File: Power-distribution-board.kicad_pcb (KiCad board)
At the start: 2 copper layers, 79 parts, among them J1 178.6165.0001 breaker, J10 2606-1104/020-000, J12 2606-1104/020-000, J13 2606-1104/020-000, J15 2606-1104/020-000, J16 2606-1104/020-000, J2 178.6165.0001 breaker, J3 178.6165.0001 breaker, J4 178.6165.0001 breaker, J5 178.6165.0001 breaker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

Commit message: work on pcb editor
changed layout of components, changed to 4 layer pcb, set minimum trace width 0.2mm
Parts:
- moved J10 212.6 mm to (254.2, 91.3), turned to 90 degrees
- moved J13 182.2 mm to (251.8, 54.4), turned to 90 degrees
- moved J6 180.9 mm to (246.2, 66.3), turned to 90 degrees
- moved J5 169.5 mm to (237.4, 66.3), turned to 90 degrees
- moved J4 169.4 mm to (246.6, 90.1), turned to 90 degrees
- moved J2 157.7 mm to (230.5, 56.1), turned to 180 degrees
- moved J12 142.6 mm to (221.9, 111.5)
- moved J3 139.9 mm to (208.3, 55.9), turned to 180 degrees
- moved J16 135.7 mm to (238.2, 50.1)
- moved J15 135.6 mm to (253.0, 126.6), turned to 90 degrees
- moved U3 124.1 mm to (214.7, 74.2), turned to 180 degrees
- moved U14 106.6 mm to (205.1, 69.0), turned to 180 degrees
- moved U12 104.5 mm to (204.1, 87.1), turned to 180 degrees
- moved U13 102.7 mm to (203.9, 81.6), turned to 180 degrees
- moved U15 101.2 mm to (215.0, 87.7), turned to 180 degrees
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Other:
- copper layers 2 -> 4

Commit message: set layout
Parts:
- moved U15 134.3 mm to (81.6, 103.1)
- moved U16 120.5 mm to (100.0, 118.9)
- moved U3 120.4 mm to (94.4, 78.3)
- moved J5 118.0 mm to (132.2, 119.6), turned to 180 degrees
- moved R45 117.9 mm to (64.2, 133.5)
- moved J9 117.4 mm to (63.0, 140.9), turned to 0 degrees
- moved U4 116.6 mm to (98.0, 141.7)
- moved U2 113.1 mm to (80.5, 138.7), turned to 180 degrees
- moved U17 108.2 mm to (94.8, 99.0)
- moved R46 104.3 mm to (61.4, 133.5)
- moved U1 100.4 mm to (70.4, 75.1), turned to 0 degrees
- moved R24 97.9 mm to (143.3, 98.9), turned to 0 degrees
- moved C5 97.7 mm to (53.6, 134.2), turned to 0 degrees
- moved U12 96.7 mm to (108.2, 99.1), turned to -90 degrees
- moved R5 94.5 mm to (56.7, 124.1), turned to 180 degrees
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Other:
- board outline added: 139.2 x 107.7 mm

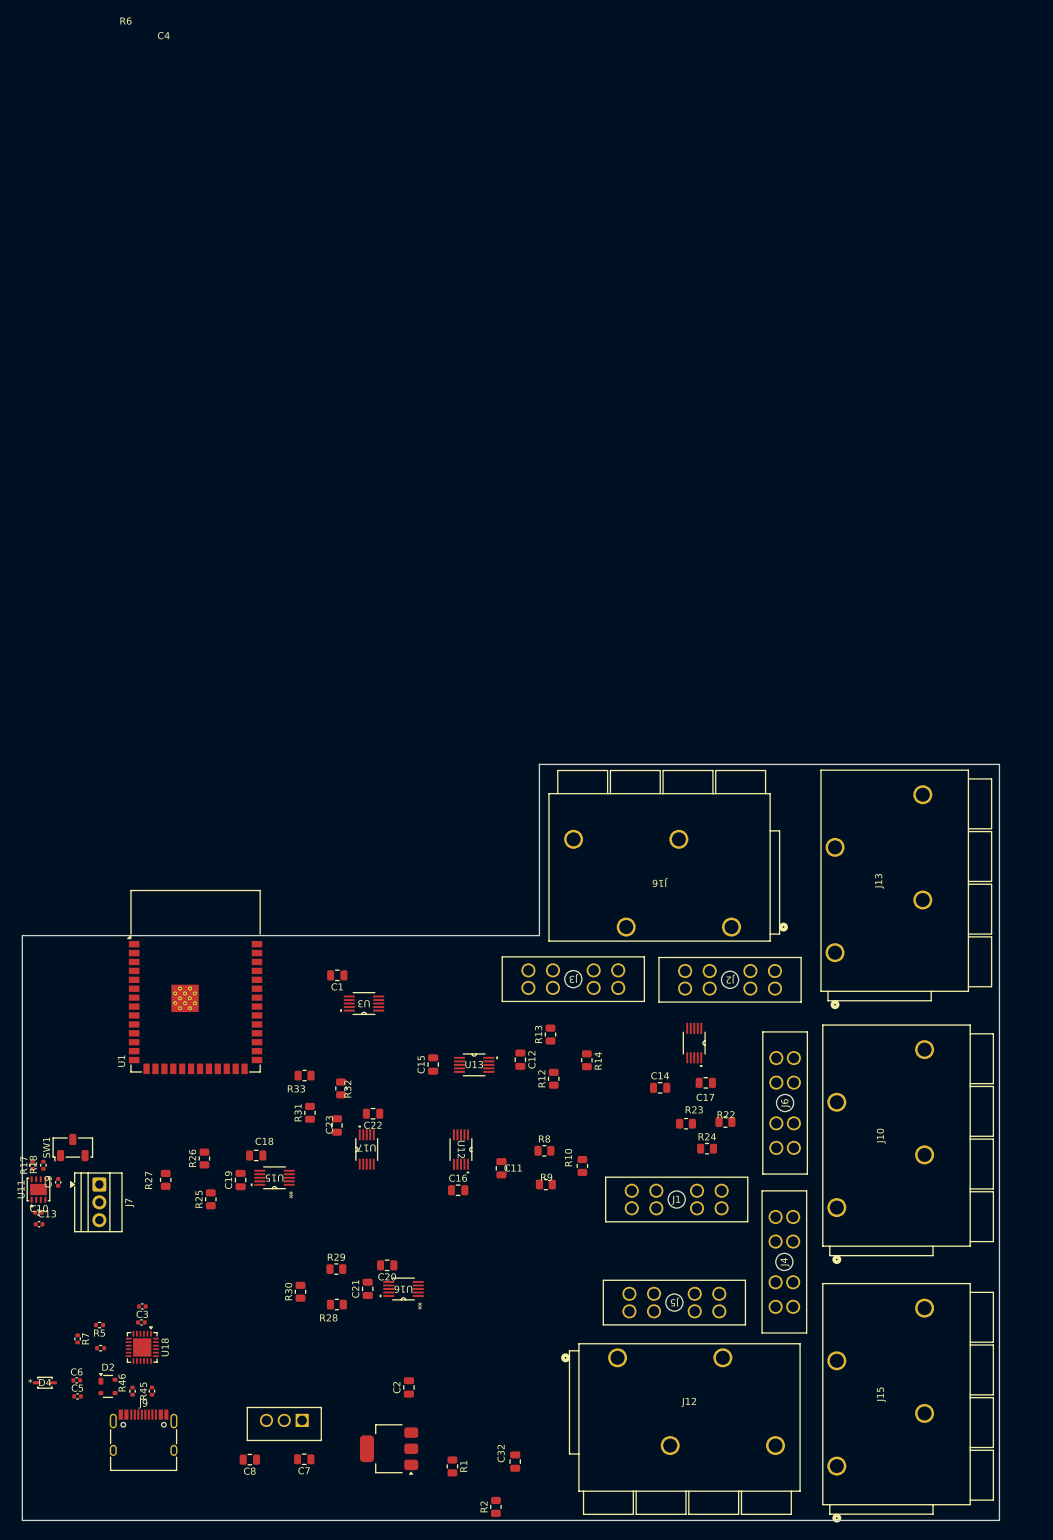
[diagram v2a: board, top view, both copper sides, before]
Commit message: update layout
added board edge and planes
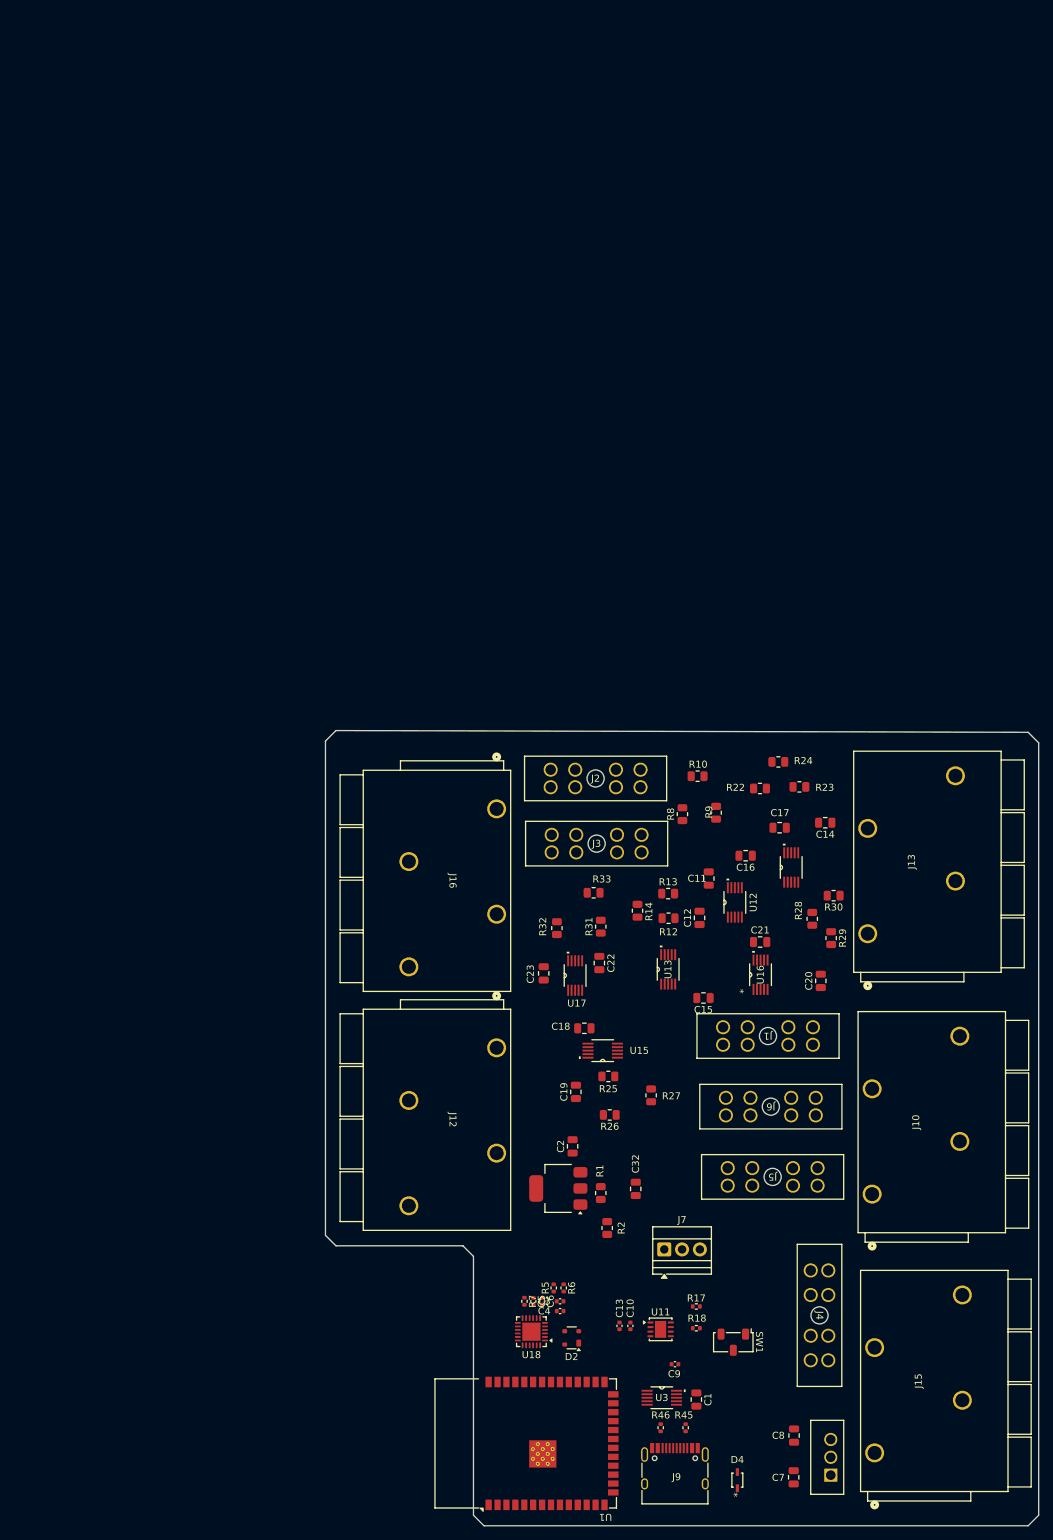
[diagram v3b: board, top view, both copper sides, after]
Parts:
- moved D4 99.6 mm to (147.6, 146.2), turned to 90 degrees
- moved SW1 98.1 mm to (147.0, 126.5), turned to -90 degrees
- moved R17 96.7 mm to (141.7, 121.4), turned to 0 degrees
- moved R18 95.9 mm to (141.7, 124.5), turned to 0 degrees
- moved R30 94.6 mm to (161.3, 62.9), turned to 180 degrees
- moved C9 91.6 mm to (138.7, 129.6), turned to 180 degrees
- moved U11 90.8 mm to (136.6, 124.7), turned to 0 degrees
- moved R28 87.2 mm to (158.2, 66.2), turned to 90 degrees
- moved C10 85.9 mm to (132.3, 124.2), turned to -90 degrees
- moved R29 84.8 mm to (160.9, 68.9), turned to -90 degrees
- moved C13 83.9 mm to (130.8, 124.2), turned to -90 degrees
- moved J7 81.0 mm to (137.2, 113.3), turned to 0 degrees
- moved U1 80.9 mm to (117.4, 140.9), turned to 90 degrees
- moved U2 79.4 mm to (159.9, 140.4), turned to 90 degrees
- moved C1 79.2 mm to (141.7, 134.7), turned to -90 degrees
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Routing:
- added copper zone on In1.Cu, net GND
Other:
- board size 139.2 x 107.7 mm -> 101.6 x 113.3 mm

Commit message: rearrangement
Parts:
- moved R5 7.55 mm to (120.8, 111.2)
- moved R6 7.55 mm to (122.2, 111.2)
- moved R7 6.57 mm to (114.3, 114.8)
- moved C5 6.04 mm to (117.1, 114.8)
- moved C6 6.00 mm to (119.9, 114.7)
- moved U18 5.62 mm to (115.9, 119.9)
- moved U1 2.74 mm to (116.5, 138.3)
- moved C3 2.60 mm to (121.9, 118.1)
- moved C4 2.60 mm to (121.9, 119.5)
- moved J16 2.02 mm to (113.3, 48.5)
- moved D2 1.28 mm to (123.4, 124.7)
- moved C15 1.02 mm to (142.7, 76.5)
- moved J9 0.16 mm to (138.8, 145.6)
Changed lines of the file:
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@@
 	)
 	(footprint "Connector_USB:USB_C_Receptacle_HRO_TYPE-C-31-M-12"
-		(locked yes)
 		(layer "F.Cu")
-		(at 138.684 145.635)
+		(at 138.842 145.602)
 		(descr "USB Type-C receptacle for USB 2.0 and PD, http://www.krhro.com/uploads/soft/180320/1-1P320120243.pdf")
 		(tags "usb usb-c 2.0 pd")
@@
 	)
 	(footprint "Package_DFN_QFN:QFN-24-1EP_4x4mm_P0.5mm_EP2.6x2.6mm"
-		(locked yes)
 		(layer "F.Cu")
-		(at 118.2336 125.0084 180)
+		(at 115.9185 119.884 180)
 		(descr "QFN, 24 Pin (http://ww1.microchip.com/downloads/en/PackagingSpec/00000049BQ.pdf#page=278), generated with kicad-footprint-generator ipc_noLead_generator.py")
 		(tags "QFN NoLead")
 		(property "Reference" "U18"
-			(at 0 -3.3 0)
+			(at -0.1595 -3.814 0)
 			(layer "F.SilkS")
 			(effects
@@
 	)
 	(footprint "Resistor_SMD:R_0402_1005Metric"
-		(locked yes)
 		(layer "F.Cu")
-		(at 121.412 118.7704 90)
+		(at 120.7502 111.25 90)
 		(descr "Resistor SMD 0402 (1005 Metric), square (rectangular) end terminal, IPC-7351 nominal, (Body size source: IPC-SM-782 page 72, https://www.pcb-3d.com/wordpress/wp-content/uploads/ipc-sm-782a_amendment_1_and_2.pdf), generated with kicad-footprint-generator")
 		(tags "resistor")
@@
 	)
 	(footprint "Resistor_SMD:R_0402_1005Metric"
-		(locked yes)
 		(layer "F.Cu")
-		(at 117.2478 120.6754 -90)
+		(at 114.3 114.808 -90)
 		(descr "Resistor SMD 0402 (1005 Metric), square (rectangular) end terminal, IPC-7351 nominal, (Body size source: IPC-SM-782 page 72, https://www.pcb-3d.com/wordpress/wp-content/uploads/ipc-sm-782a_amendment_1_and_2.pdf), generated with kicad-footprint-generator")
 		(tags "resistor")
 		(property "Reference" "R7"
-			(at 0 -1.17 90)
+			(at -2.286 0 270)
 			(layer "F.SilkS")
 			(effects
@@
 	)
 	(footprint "Resistor_SMD:R_0402_1005Metric"
-		(locked yes)
 		(layer "F.Cu")
-		(at 122.8358 118.7704 -90)
+		(at 122.174 111.25 -90)
 		(descr "Resistor SMD 0402 (1005 Metric), square (rectangular) end terminal, IPC-7351 nominal, (Body size source: IPC-SM-782 page 72, https://www.pcb-3d.com/wordpress/wp-content/uploads/ipc-sm-782a_amendment_1_and_2.pdf), generated with kicad-footprint-generator")
 		(tags "resistor")
@@
 	)
 	(footprint "Package_TO_SOT_SMD:SOT-143"
-		(locked yes)
 		(layer "F.Cu")
-		(at 123.9788 125.8824 180)
+		(at 123.444 124.714 180)
 		(descr "SOT-143 https://www.nxp.com/docs/en/package-information/SOT143B.pdf")
 		(tags "SOT-143")
@@
 	)
 	(footprint "Capacitor_SMD:C_0402_1005Metric"
-		(locked yes)
 		(layer "F.Cu")
-		(at 122.3278 122.0724 180)
+		(at 121.92 119.507 180)
 		(descr "Capacitor SMD 0402 (1005 Metric), square (rectangular) end terminal, IPC-7351 nominal, (Body size source: IPC-SM-782 page 76, https://www.pcb-3d.com/wordpress/wp-content/uploads/ipc-sm-782a_amendment_1_and_2.pdf), generated with kicad-footprint-generator")
 		(tags "capacitor")
 		(property "Reference" "C4"
-			(at 2.258 0 0)
+			(at -2.286 0.127 0)
 			(layer "F.SilkS")
 			(effects
@@
 		(tags "INA220BIDGSR ")
 		(property "Reference" "U14"
-			(at -0.5461 -3.438401 270)
+			(at 0.2032 2.7432 90)
 			(unlocked yes)
-			(layer "B.SilkS")
+			(layer "F.SilkS")
 			(effects
 				(font
@@
 					(thickness 0.15)
 				)
-				(justify mirror)
 			)
 		)
@@
 	(footprint "Capacitor_SMD:C_0805_2012Metric"
 		(layer "F.Cu")
-		(at 142.748 77.47 180)
+		(at 142.748 76.454 180)
 		(descr "Capacitor SMD 0805 (2012 Metric), square (rectangular) end terminal, IPC-7351 nominal, (Body size source: IPC-SM-782 page 76, https://www.pcb-3d.com/wordpress/wp-content/uploads/ipc-sm-782a_amendment_1_and_2.pdf, https://docs.google.com/spreadsheets/d/1BsfQQcO9C6DZCsRaXUlFlo91Tg2WpOkGARC1WS5S8t0/edit?usp=sharing), generated with kicad-footprint-generator")
 		(tags "capacitor")
@@
 	)
 	(footprint "Capacitor_SMD:C_0402_1005Metric"
-		(locked yes)
 		(layer "F.Cu")
-		(at 118.5178 120.6754 -90)
+		(at 117.094 114.808 -90)
 		(descr "Capacitor SMD 0402 (1005 Metric), square (rectangular) end terminal, IPC-7351 nominal, (Body size source: IPC-SM-782 page 76, https://www.pcb-3d.com/wordpress/wp-content/uploads/ipc-sm-782a_amendment_1_and_2.pdf), generated with kicad-footprint-generator")
 		(tags "capacitor")
 		(property "Reference" "C5"
-			(at 0 -1.16 90)
+			(at -2.286 0 270)
 			(layer "F.SilkS")
 			(effects
@@
 	)
 	(footprint "Capacitor_SMD:C_0402_1005Metric"
-		(locked yes)
 		(layer "F.Cu")
-		(at 122.3278 120.6754 180)
+		(at 121.92 118.11 180)
 		(descr "Capacitor SMD 0402 (1005 Metric), square (rectangular) end terminal, IPC-7351 nominal, (Body size source: IPC-SM-782 page 76, https://www.pcb-3d.com/wordpress/wp-content/uploads/ipc-sm-782a_amendment_1_and_2.pdf), generated with kicad-footprint-generator")
 		(tags "capacitor")
 		(property "Reference" "C3"
-			(at 2.258 0 0)
+			(at -2.286 0.127 0)
 			(layer "F.SilkS")
 			(effects
@@
 	)
 	(footprint "RF_Module:ESP32-S3-WROOM-1"
-		(locked yes)
 		(layer "F.Cu")
-		(at 117.3996 140.9208 90)
+		(at 116.512 138.33 90)
 		(descr "2.4 GHz Wi-Fi and Bluetooth module  https://www.espressif.com/sites/default/files/documentation/esp32-s3-wroom-1_wroom-1u_datasheet_en.pdf")
 		(tags "2.4 GHz Wi-Fi and Bluetooth module")
@@
 			(polygon
 				(pts
-					(xy 110.6496 164.9208) (xy 110.6496 116.9208) (xy 89.6496 116.9208) (xy 89.6496 164.9208)
+					(xy 109.762 162.33) (xy 109.762 114.33) (xy 88.762 114.33) (xy 88.762 162.33)
 				)
 			)
@@
 	)
 	(footprint "Capacitor_SMD:C_0402_1005Metric"
-		(locked yes)
 		(layer "F.Cu")
-		(at 119.7878 120.6754 -90)
+		(at 119.888 114.679 -90)
 		(descr "Capacitor SMD 0402 (1005 Metric), square (rectangular) end terminal, IPC-7351 nominal, (Body size source: IPC-SM-782 page 76, https://www.pcb-3d.com/wordpress/wp-content/uploads/ipc-sm-782a_amendment_1_and_2.pdf), generated with kicad-footprint-generator")
 		(tags "capacitor")
@@
 	)
 	(footprint "pdb_footprints:CONN4_2606-1104&slash_020-000_WAG"
-		(locked yes)
 		(layer "F.Cu")
-		(at 113.284 50.531999 -90)
+		(at 113.284 48.5129 -90)
 		(tags "2606-1104/020-000 ")
 		(property "Reference" "J16"
